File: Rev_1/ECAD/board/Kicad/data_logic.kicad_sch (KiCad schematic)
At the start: 67 parts, among them SW300 SW_Push, SW301 SW_Push, SW302 SW_Push, SW303 SW_Push

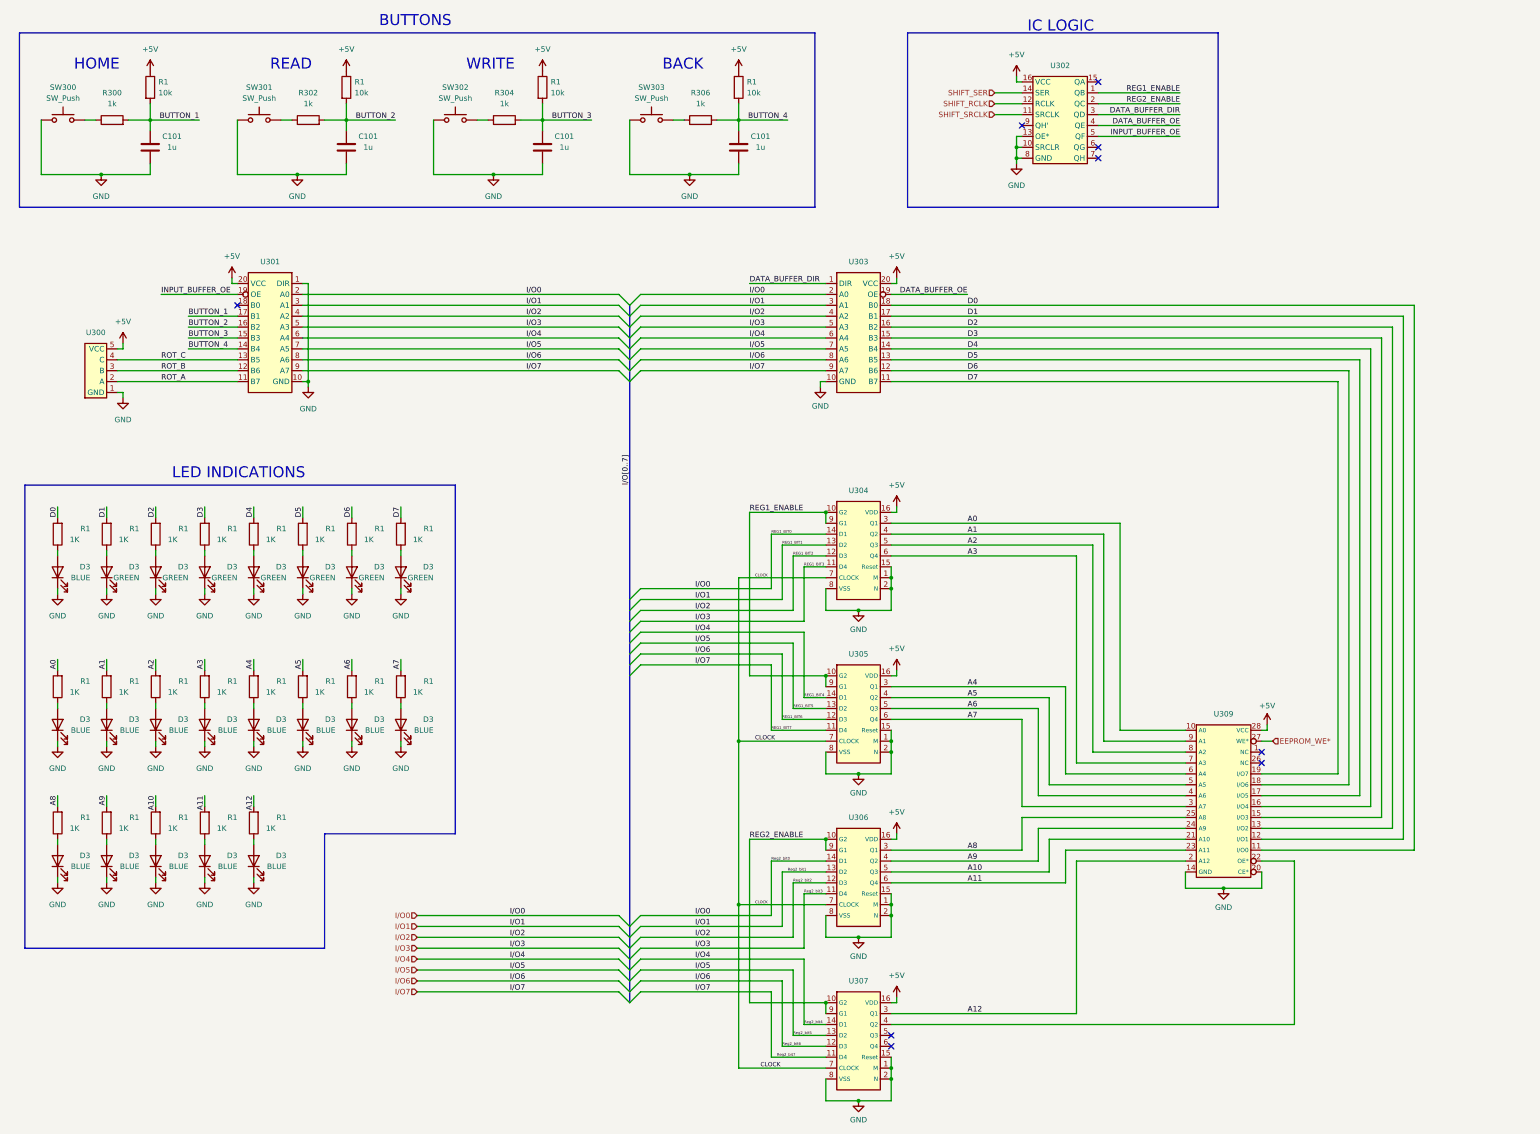
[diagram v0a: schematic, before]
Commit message: Updated Symbol library´and added SD Card Reader to schematic
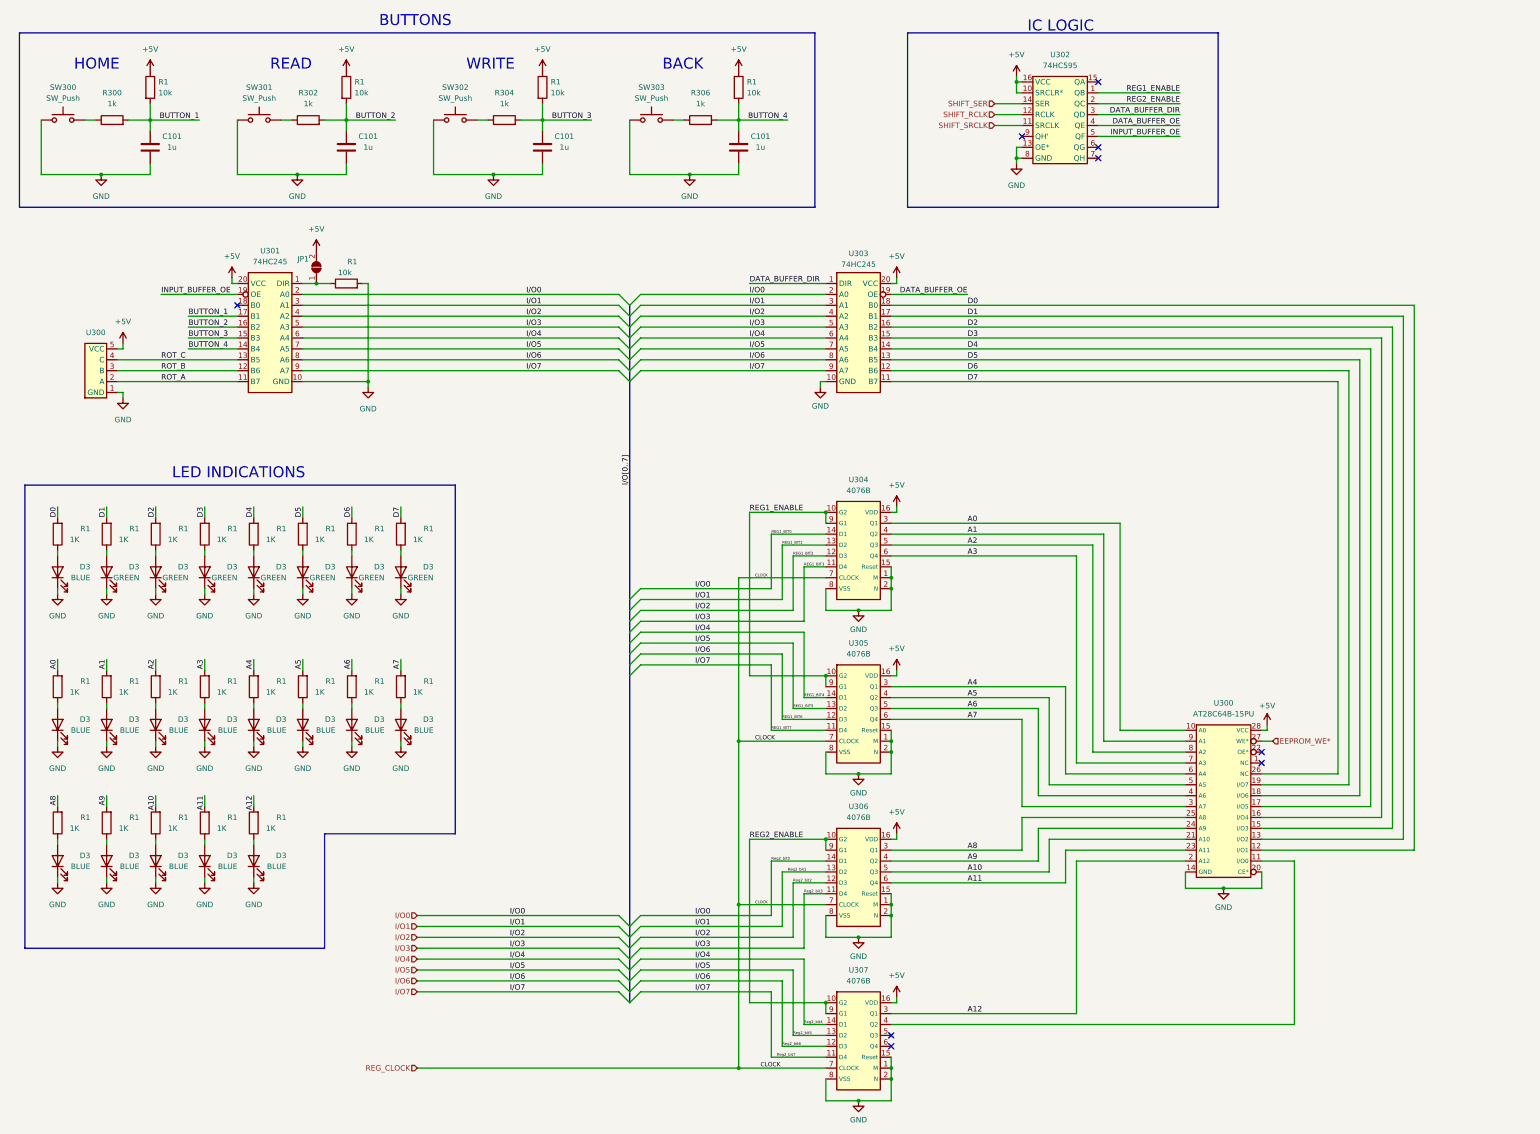
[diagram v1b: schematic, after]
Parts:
- removed U301, U303: ~, symbol EEPROM_PROGRAMER:74HC245
- removed U302: ~, symbol EEPROM_PROGRAMER:74HC595
- removed U309: ~, symbol EEPROM_PROGRAMER:AT28C64B-15PU
- added JP1: SolderJumper_2_Open, Jumper:SolderJumper-2_P1.3mm_Open_Pad1.0x1.5mm, symbol Jumper:SolderJumper_2_Open
- added R1: 10k, Resistor_SMD:R_0805_2012Metric_Pad1.20x1.40mm_HandSolder, symbol Device:R
- added U300: AT28C64B-15PU, symbol EEPROM_PROGRAMMER:AT28C64B-15PU
- added U301, U303: 74HC245, symbol EEPROM_PROGRAMMER:74HC245
- added U302: 74HC595, symbol EEPROM_PROGRAMMER:74HC595
- U304, U305, U306, U307: value ~ -> 4076B
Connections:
- net +5V: now also JP1.2 (B), U300.28 (VCC), U301.20 (VCC), U302.10 (SRCLR*), U302.16 (VCC), U303.20 (VCC)
- net A0: now also U300.10 (A0)
- net A1: now also U300.9 (A1)
- net A10: now also U300.21 (A10)
- net A11: now also U300.23 (A11)
- net A12: now also U300.2 (A12)
- net A2: now also U300.8 (A2)
- net A3: now also U300.7 (A3)
- net A4: now also U300.6 (A4)
- net A5: now also U300.5 (A5)
- net A6: now also U300.4 (A6)
- net A7: now also U300.3 (A7)
- net A8: now also U300.25 (A8)
- net A9: now also U300.24 (A9)
- net BUTTON_1: now also U301.17 (B1)
- net BUTTON_2: now also U301.16 (B2)
- net BUTTON_3: now also U301.15 (B3)
- net BUTTON_4: now also U301.14 (B4)
- net D0: now also U300.12 (I/O1), U303.18 (B0)
- net D1: now also U300.13 (I/O2), U303.17 (B1)
- net D2: now also U300.15 (I/O3), U303.16 (B2)
- net D3: now also U300.16 (I/O4), U303.15 (B3)
- net D4: now also U300.17 (I/O5), U303.14 (B4)
- net D5: now also U300.18 (I/O6), U303.13 (B5)
- net D6: now also U300.19 (I/O7), U303.12 (B6)
- net D7: now also U300.26 (NC), U303.11 (B7)
- net DATA_BUFFER_DIR: now also U302.3 (QD), U303.1 (DIR)
- net DATA_BUFFER_OE: now also U302.4 (QE), U303.19 (OE)
- net EEPROM_WE*: now also U300.27 (WE*)
- net GND: now also R1.2, U300.14 (GND), U300.20 (CE*), U301.10 (GND), U302.13 (OE*), U302.8 (GND), U303.10 (GND)
- net INPUT_BUFFER_OE: now also U301.19 (OE), U302.5 (QF)
- net I/O0: now also U301.2 (A0), U303.2 (A0)
- net I/O1: now also U301.3 (A1), U303.3 (A1)
- net I/O2: now also U301.4 (A2), U303.4 (A2)
- net I/O3: now also U301.5 (A3), U303.5 (A3)
- net I/O4: now also U301.6 (A4), U303.6 (A4)
- net I/O5: now also U301.7 (A5), U303.7 (A5)
- net I/O6: now also U301.8 (A6), U303.8 (A6)
- net I/O7: now also U301.9 (A7), U303.9 (A7)
- net REG1_ENABLE: now also U302.1 (QB)
- net REG2_ENABLE: now also U302.2 (QC)
- net ROT_A: now also U301.11 (B7)
- net ROT_B: now also U301.12 (B6)
- net ROT_C: now also U301.13 (B5)
- net SHIFT_RCLK: now also U302.12 (RCLK)
- net SHIFT_SER: now also U302.14 (SER)
- net SHIFT_SRCLK: now also U302.11 (SRCLK)
- net at U307.4 (Q2): now also U300.11 (I/O0)
- net CLOCK renamed REG_CLOCK
- new net: JP1.1 (A), R1.1, U301.1 (DIR)

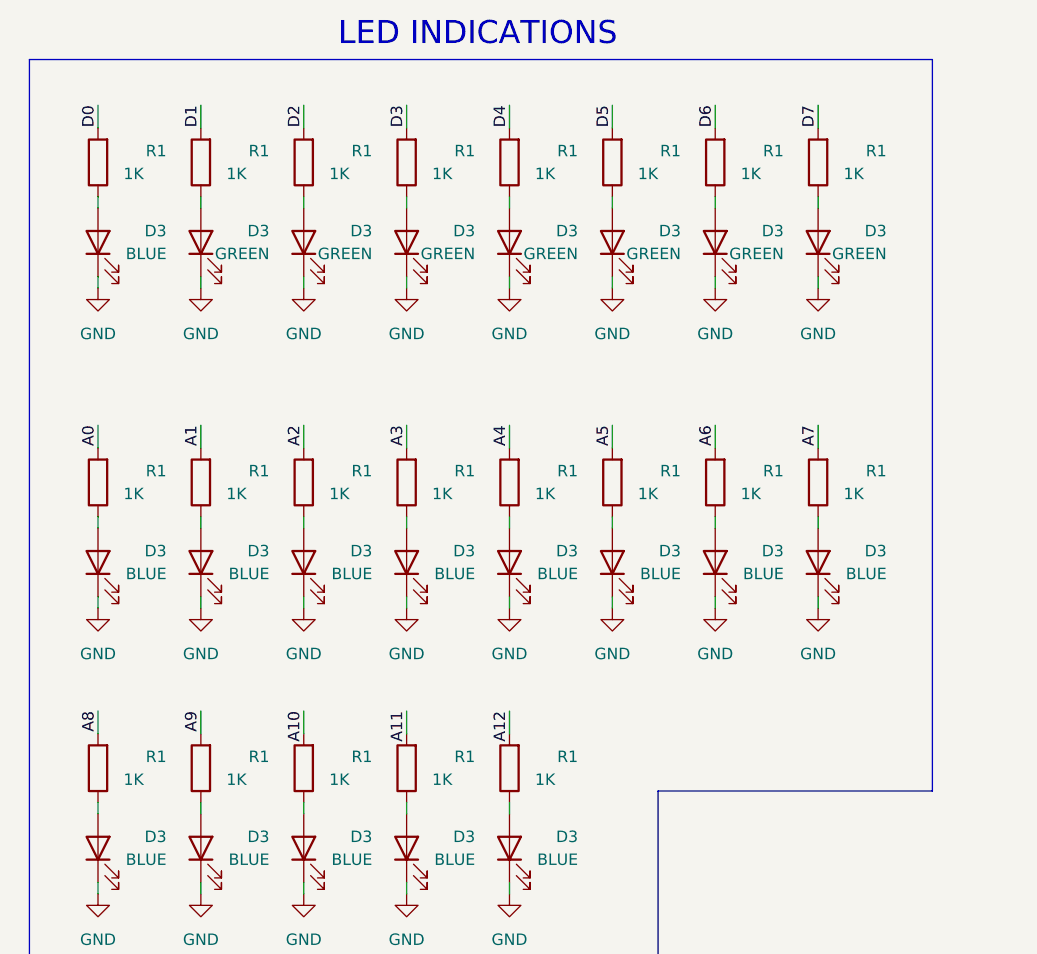
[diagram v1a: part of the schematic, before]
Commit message: Changes current limiting resistors for LEDS to 5k1 ohms
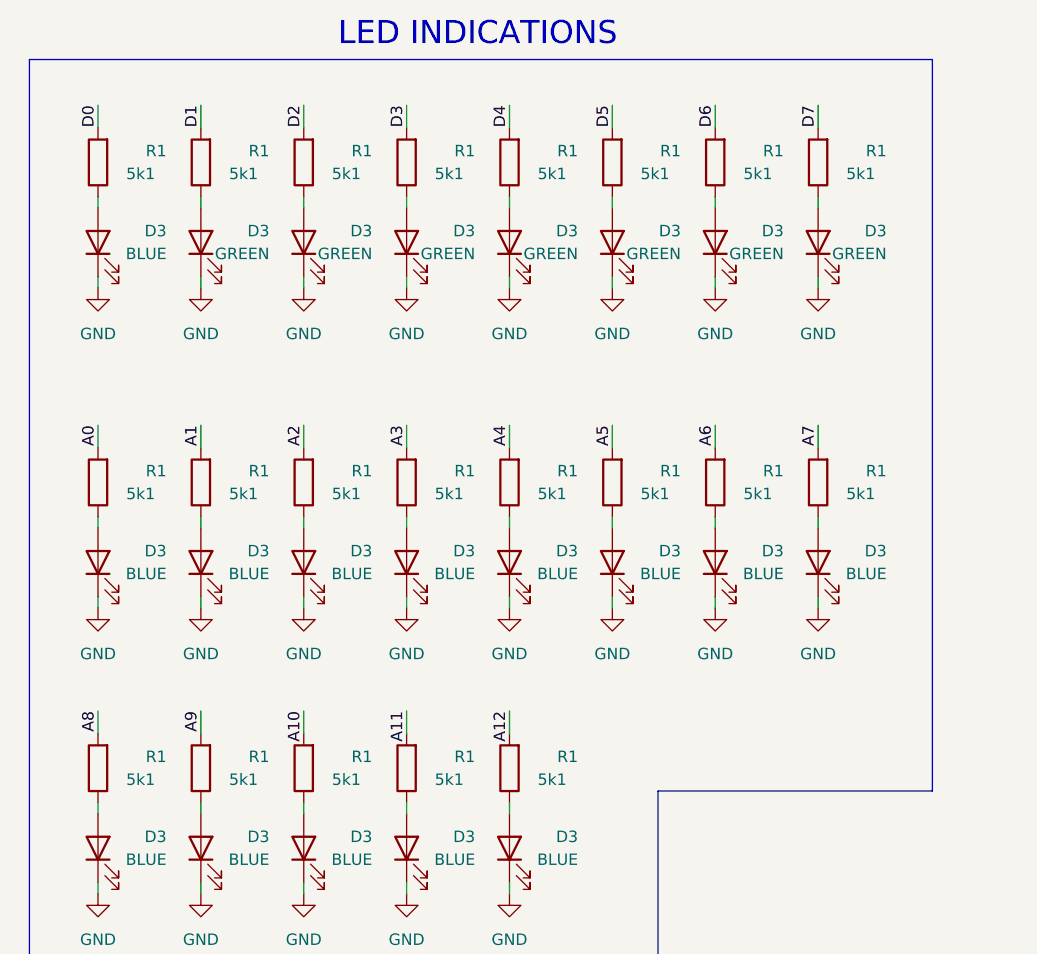
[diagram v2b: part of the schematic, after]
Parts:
- R1: value 1K -> 5k1
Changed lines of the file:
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@@
       (effects (font (size 1.27 1.27)) (justify left))
     )
-    (property "Value" "1K" (at 45.72 171.45 0)
+    (property "Value" "5k1" (at 46.99 171.45 0)
       (effects (font (size 1.27 1.27)) (justify left))
     )
@@
       (effects (font (size 1.27 1.27)) (justify left))
     )
-    (property "Value" "1K" (at 68.58 203.2 0)
+    (property "Value" "5k1" (at 69.85 203.2 0)
       (effects (font (size 1.27 1.27)) (justify left))
     )
@@
       (effects (font (size 1.27 1.27)) (justify left))
     )
-    (property "Value" "1K" (at 34.29 203.2 0)
+    (property "Value" "5k1" (at 35.56 203.2 0)
       (effects (font (size 1.27 1.27)) (justify left))
     )
@@
       (effects (font (size 1.27 1.27)) (justify left))
     )
-    (property "Value" "1K" (at 91.44 135.89 0)
+    (property "Value" "5k1" (at 92.71 135.89 0)
       (effects (font (size 1.27 1.27)) (justify left))
     )
@@
       (effects (font (size 1.27 1.27)) (justify left))
     )
-    (property "Value" "1K" (at 80.01 203.2 0)
+    (property "Value" "5k1" (at 81.28 203.2 0)
       (effects (font (size 1.27 1.27)) (justify left))
     )
@@
       (effects (font (size 1.27 1.27)) (justify left))
     )
-    (property "Value" "1K" (at 80.01 171.45 0)
+    (property "Value" "5k1" (at 81.28 171.45 0)
       (effects (font (size 1.27 1.27)) (justify left))
     )
@@
       (effects (font (size 1.27 1.27)) (justify left))
     )
-    (property "Value" "1K" (at 114.3 135.89 0)
+    (property "Value" "5k1" (at 115.57 135.89 0)
       (effects (font (size 1.27 1.27)) (justify left))
     )
@@
       (effects (font (size 1.27 1.27)) (justify left))
     )
-    (property "Value" "1K" (at 34.29 171.45 0)
+    (property "Value" "5k1" (at 35.56 171.45 0)
       (effects (font (size 1.27 1.27)) (justify left))
     )
@@
       (effects (font (size 1.27 1.27)) (justify left))
     )
-    (property "Value" "1K" (at 114.3 171.45 0)
+    (property "Value" "5k1" (at 115.57 171.45 0)
       (effects (font (size 1.27 1.27)) (justify left))
     )
@@
       (effects (font (size 1.27 1.27)) (justify left))
     )
-    (property "Value" "1K" (at 102.87 135.89 0)
+    (property "Value" "5k1" (at 104.14 135.89 0)
       (effects (font (size 1.27 1.27)) (justify left))
     )
@@
       (effects (font (size 1.27 1.27)) (justify left))
     )
-    (property "Value" "1K" (at 45.72 135.89 0)
+    (property "Value" "5k1" (at 46.99 135.89 0)
       (effects (font (size 1.27 1.27)) (justify left))
     )
@@
       (effects (font (size 1.27 1.27)) (justify left))
     )
-    (property "Value" "1K" (at 102.87 171.45 0)
+    (property "Value" "5k1" (at 104.14 171.45 0)
       (effects (font (size 1.27 1.27)) (justify left))
     )
@@
       (effects (font (size 1.27 1.27)) (justify left))
     )
-    (property "Value" "1K" (at 57.15 203.2 0)
+    (property "Value" "5k1" (at 58.42 203.2 0)
       (effects (font (size 1.27 1.27)) (justify left))
     )
@@
       (effects (font (size 1.27 1.27)) (justify left))
     )
-    (property "Value" "1K" (at 80.01 135.89 0)
+    (property "Value" "5k1" (at 81.28 135.89 0)
       (effects (font (size 1.27 1.27)) (justify left))
     )
@@
       (effects (font (size 1.27 1.27)) (justify left))
     )
-    (property "Value" "1K" (at 68.58 135.89 0)
+    (property "Value" "5k1" (at 69.85 135.89 0)
       (effects (font (size 1.27 1.27)) (justify left))
     )
@@
       (effects (font (size 1.27 1.27)) (justify left))
     )
-    (property "Value" "1K" (at 57.15 171.45 0)
+    (property "Value" "5k1" (at 58.42 171.45 0)
       (effects (font (size 1.27 1.27)) (justify left))
     )
@@
       (effects (font (size 1.27 1.27)) (justify left))
     )
-    (property "Value" "1K" (at 45.72 203.2 0)
+    (property "Value" "5k1" (at 46.99 203.2 0)
       (effects (font (size 1.27 1.27)) (justify left))
     )
@@
       (effects (font (size 1.27 1.27)) (justify left))
     )
-    (property "Value" "1K" (at 34.29 135.89 0)
+    (property "Value" "5k1" (at 35.56 135.89 0)
       (effects (font (size 1.27 1.27)) (justify left))
     )
@@
       (effects (font (size 1.27 1.27)) (justify left))
     )
-    (property "Value" "1K" (at 68.58 171.45 0)
+    (property "Value" "5k1" (at 69.85 171.45 0)
       (effects (font (size 1.27 1.27)) (justify left))
     )
@@
       (effects (font (size 1.27 1.27)) (justify left))
     )
-    (property "Value" "1K" (at 91.44 171.45 0)
+    (property "Value" "5k1" (at 92.71 171.45 0)
       (effects (font (size 1.27 1.27)) (justify left))
     )
@@
       (effects (font (size 1.27 1.27)) (justify left))
     )
-    (property "Value" "1K" (at 57.15 135.89 0)
-      (effects (font (size 1.27 1.27)) (justify left))
-    )
+    (property "Value" "5k1" (at 58.42 135.89 0)
+      (effects (font (size 1.27 1.27)) (justify left))
+    )
